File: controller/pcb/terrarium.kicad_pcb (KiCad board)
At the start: 4 copper layers, 90 x 90 mm, 83 parts, among them K1 G3MB-202P, K2 G3MB-202P, K3 G3MB-202P, P1 USB_C_Plug_USB2.0, Q1 S8050, Q2 S8050, Q3 S8050, Q4 S8050, Q5 s8050, Q6 s8050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

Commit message: pcb v1.7 done
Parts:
- added LED8: LED, Connector_JST:JST_XH_B3B-XH-A_1x03_P2.50mm_Vertical, F.Cu at (47.0, 38.1)
- added RESET_EEPROM1: data, Connector_PinHeader_2.54mm:PinHeader_1x01_P2.54mm_Vertical, F.Cu at (96.5, 75.4)
- added U6: CAT24C256, Package_DIP:DIP-8_W7.62mm_Socket, F.Cu at (55.9, 47.0)
- moved ALED1 10.9 mm to (56.5, 32.7)
- moved C1 10.9 mm to (56.5, 27.8)
- moved R5 10.9 mm to (56.5, 37.8)
- moved G*** 6.56 mm to (73.3, 64.0)
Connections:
- U1 pad 23: Net-(U1-Pad23) -> G2
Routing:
- net G2: track 0.00 -> 19.2 mm, vias 0 -> 2
- net SCL: track 110.7 -> 129.7 mm
- net Net-(ALED1-Pad2): track 0.00 -> 18.8 mm, vias 0 -> 1
- net SDA: track 120.1 -> 138.6 mm
- net G23: track 88.3 -> 83.0 mm
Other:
- board text added: "220v out 1"
- board text added: "220v out 2"
- board text added: "220v out 3"
- board text added: "terrarium controller v1.7 github.com/brushknight/terrarium github.com/brushknight/terrarium-hardware"
- board text removed: "Heater 1"
- board text removed: "Heater 2"
- board text removed: "Lamp 1"
- board text removed: "terrarium controller v1.6 github.com/brushknight/terrarium github.com/brushknight/terrarium-hardware"

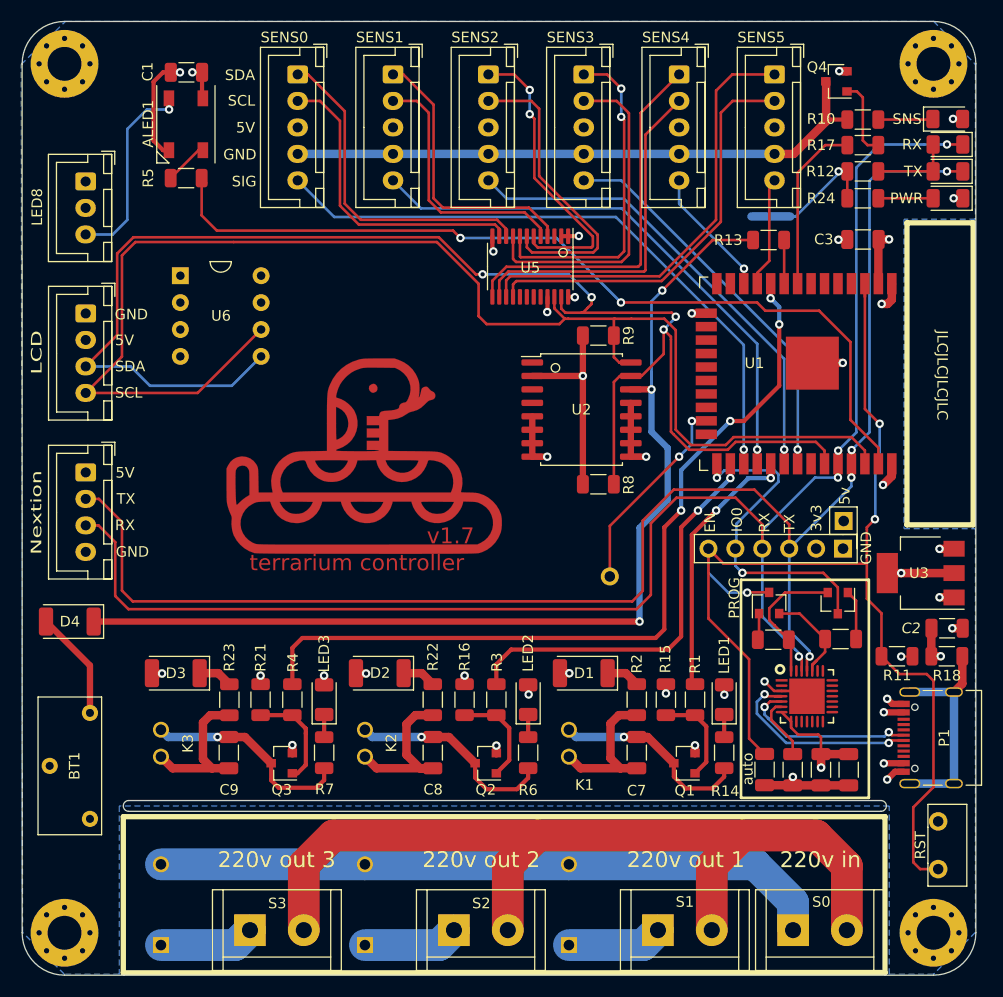
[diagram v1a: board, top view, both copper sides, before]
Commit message: change programming header to test pads
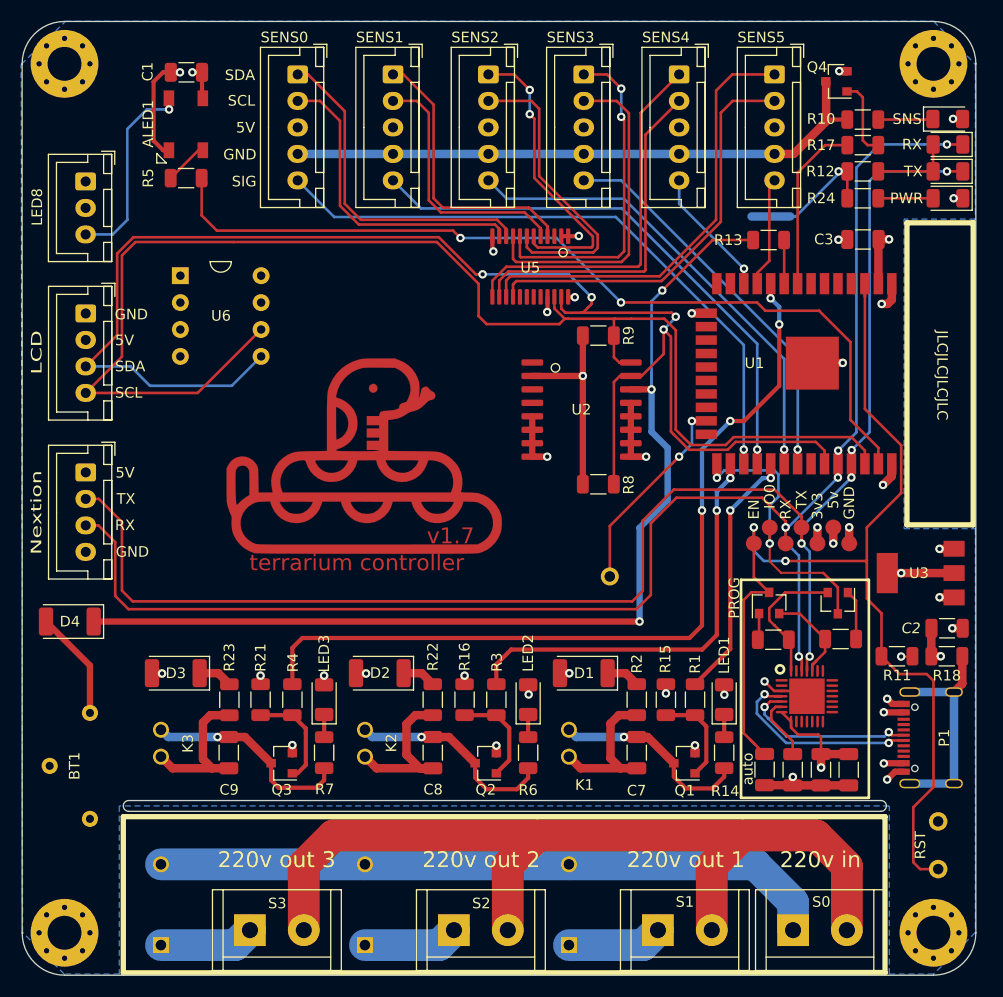
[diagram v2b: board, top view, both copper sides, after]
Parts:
- removed PWR1: data, Connector_PinHeader_2.54mm:PinHeader_1x01_P2.54mm_Vertical
- removed UART1: data, Connector_PinHeader_2.54mm:PinHeader_1x06_P2.54mm_Vertical
- added TP_3V3: TestPoint, TestPoint:TestPoint_Pad_1.5x1.5mm, F.Cu at (144.0, 73.6)
- added TP_5V1: TestPoint, TestPoint:TestPoint_Pad_1.5x1.5mm, F.Cu at (114.3, 72.1)
- added TP_EN1: TestPoint, TestPoint:TestPoint_Pad_1.5x1.5mm, F.Cu at (109.7, 72.4)
- added TP_GND1: TestPoint, TestPoint:TestPoint_Pad_1.5x1.5mm, F.Cu at (116.6, 73.9)
- added TP_IO0: TestPoint, TestPoint:TestPoint_Pad_1.5x1.5mm, F.Cu at (110.0, 70.6)
- added TP_RX1: TestPoint, TestPoint:TestPoint_Pad_1.5x1.5mm, F.Cu at (111.5, 72.4)
- added TP_TX1: TestPoint, TestPoint:TestPoint_Pad_1.5x1.5mm, F.Cu at (111.5, 72.1)
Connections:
- U6 pad 7: Net-(U6-Pad7) -> GND
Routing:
- net EN: track 110.4 -> 104.8 mm, vias 3 -> 2
- net IO0: track 30.9 -> 27.6 mm
- net G4: track 38.6 -> 40.5 mm
- net G25: track 77.5 -> 79.3 mm
- net GND: track 67.6 -> 69.1 mm, vias 25 -> 26
- net +5V: track 26.5 -> 28.0 mm, vias 13 -> 14
- net +3V3: track 45.7 -> 46.9 mm, vias 6 -> 7
- net G5: track 25.3 -> 24.2 mm
- net RX: track 146.7 -> 145.6 mm, vias 4 -> 5
- net TX: track 145.5 -> 145.7 mm, vias 4 -> 5

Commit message: rearrage some components
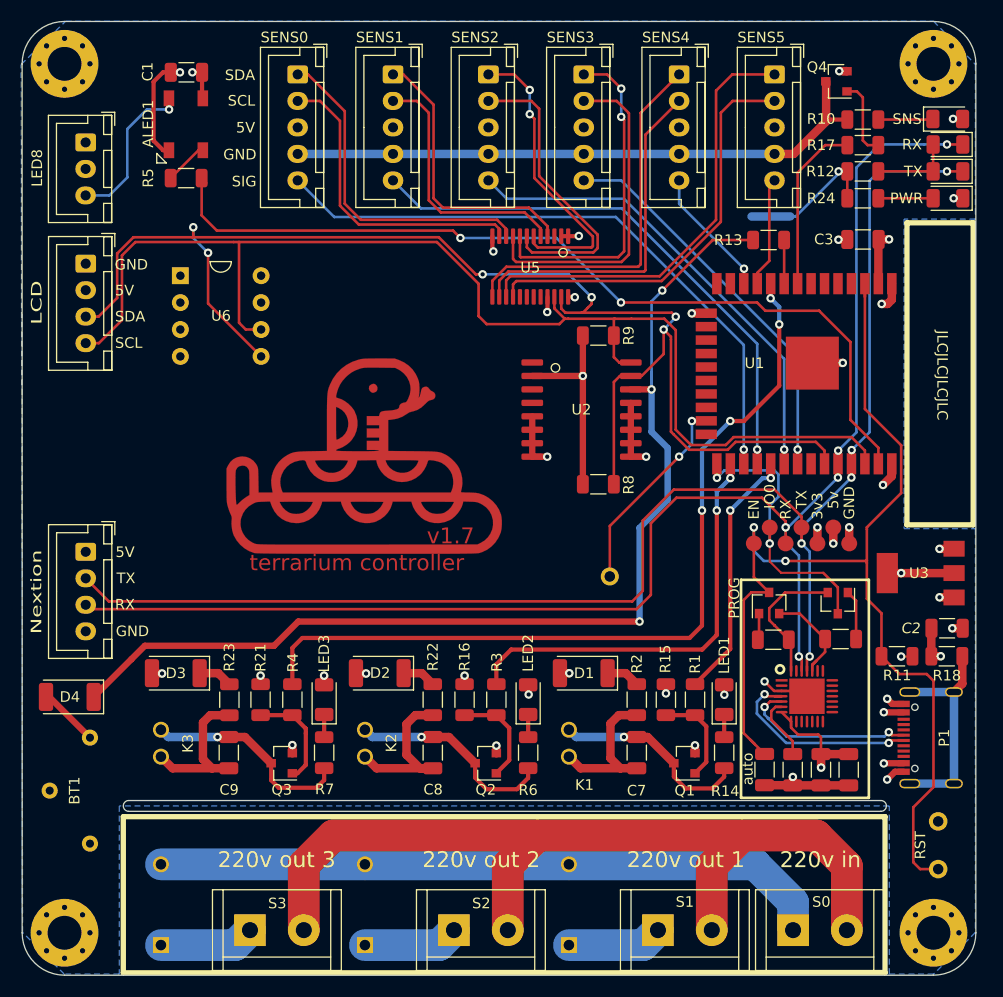
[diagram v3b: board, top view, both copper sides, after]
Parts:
- moved TP_3V3 27.9 mm to (116.0, 73.6)
- moved UART2 7.49 mm to (47.0, 73.0)
- moved D4 7.11 mm to (45.5, 86.7)
- moved I2C1 4.70 mm to (47.0, 45.9)
- moved LED8 3.68 mm to (47.0, 34.4)
- moved BT1 2.33 mm to (45.5, 95.6)
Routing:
- net SCL: track 129.7 -> 116.7 mm
- net TX: track 145.7 -> 138.8 mm
- net SDA: track 138.6 -> 132.0 mm, vias 4 -> 6
- net RX: track 145.6 -> 139.5 mm
- net Net-(BT1-Pad1): track 10.3 -> 5.74 mm
- net Net-(ALED1-Pad2): track 18.8 -> 15.0 mm
- net Net-(D4-Pad1): track 98.4 -> 101.4 mm

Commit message: improved silk screen, tracing
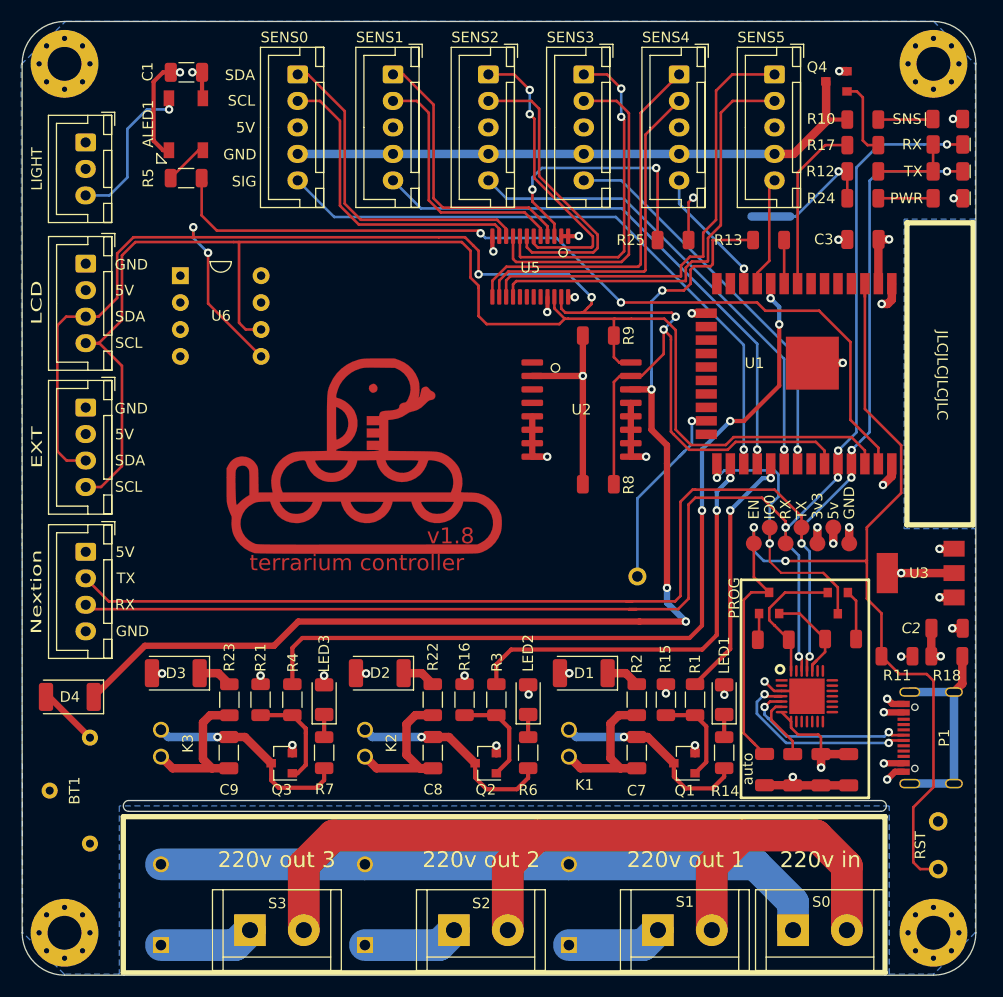
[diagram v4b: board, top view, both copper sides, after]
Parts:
- added I2C2: EXT, Connector_JST:JST_XH_B4B-XH-A_1x04_P2.50mm_Vertical, F.Cu at (47.0, 59.4)
- added R25: 10k, Resistor_SMD:R_1206_3216Metric, F.Cu at (102.4, 43.6)
- LED8: value LED -> LIGHT
- moved RESET_EEPROM1 2.60 mm to (99.1, 75.4)
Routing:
- net Net-(R25-Pad2): track 0.00 -> 25.3 mm, vias 0 -> 2
- net SCL: track 116.7 -> 136.1 mm
- net SDA: track 132.0 -> 151.2 mm
- net Net-(D4-Pad1): track 101.4 -> 107.5 mm, vias 3 -> 4
- net +3V3: track 46.9 -> 51.1 mm, vias 7 -> 8
- net SCL_5: track 39.1 -> 41.2 mm
- net RX: track 139.5 -> 141.5 mm
- net SDA_5: track 42.1 -> 44.0 mm
- net TX: track 138.8 -> 140.7 mm
- net G2: track 19.2 -> 18.8 mm, vias 2 -> 1
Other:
- board text added: "v1.8"
- board text removed: "v1.7"
